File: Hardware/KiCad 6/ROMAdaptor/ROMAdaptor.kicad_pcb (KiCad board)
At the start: 2 copper layers, 29.2 x 43.2 mm, 4 parts, among them J1 Conn_01x16, J2 Conn_01x16, U1 SST39SF040

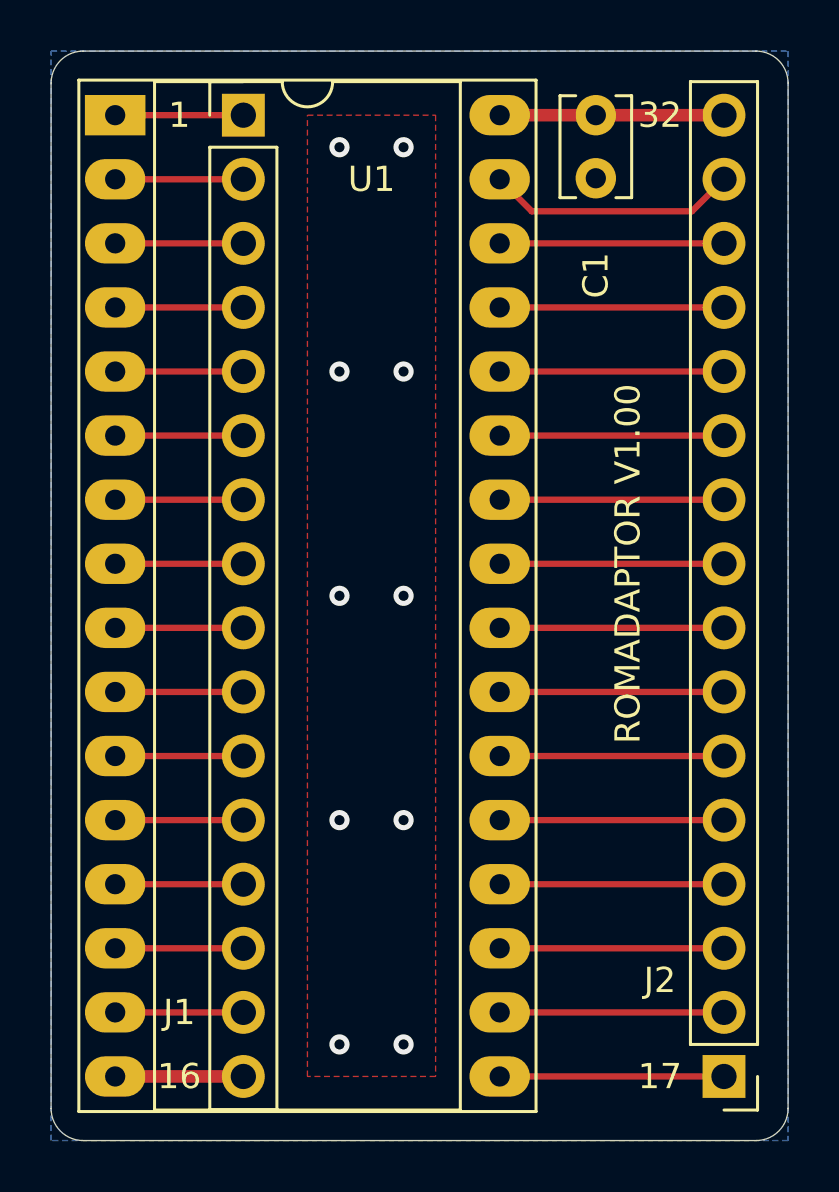
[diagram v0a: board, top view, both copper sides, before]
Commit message: Adjust orientation of ROMAdaptor headers
Flip the pin headers to the bottom of the board, to better reflect their actual position when assembled. General cleanup of disconnected traces.
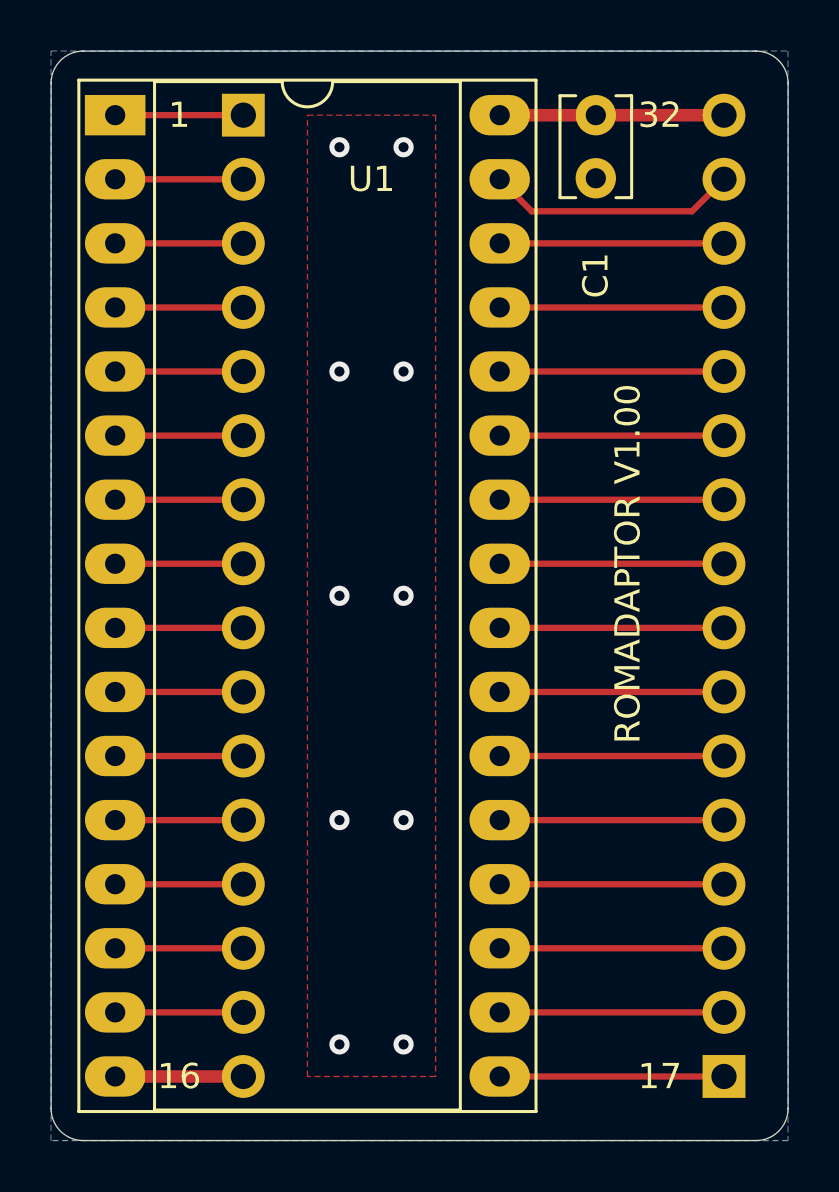
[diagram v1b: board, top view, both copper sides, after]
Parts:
- J1, J2: moved to B.Cu
- turned J1 to 180 degrees
- turned J2 to 0 degrees
